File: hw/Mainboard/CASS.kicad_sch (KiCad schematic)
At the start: 22 parts, among them J27 CASS_A_HEADER, J28 CASS_B_HEADER, J5 CASS A, J6 CASS B, Q1 AO3401A, Q3 AO3401A

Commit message: hw: add more Mouse part numbers
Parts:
- J27, J28: MOUSER (none) -> 649-1012937893602BLF
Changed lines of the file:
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@@
+      (effects (font (size 1.27 1.27)) hide)
+    )
+    (property "MOUSER" "649-1012937893602BLF" (id 4) (at 195.58 44.45 0)
       (effects (font (size 1.27 1.27)) hide)
     )
@@
       (effects (font (size 1.27 1.27)) hide)
     )
+    (property "MOUSER" "649-1012937893602BLF" (id 4) (at 241.3 44.45 0)
+      (effects (font (size 1.27 1.27)) hide)
+    )

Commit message: hw: 9V DC plug on left edge, change default track size
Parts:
- renumbered D6 to D12, D7 to D13, J27 to J14, J28 to J15, J5 to J16, J6 to J17, JP5 to JP2, JP6 to JP3, JP3 to JP4, JP4 to JP5, JP1 to JP6, JP2 to JP7, PT21 to PT38, PT15 to PT39, PT16 to PT40, PT22 to PT41, Q3 to Q2, Q1 to Q3, R50 to R31, R56 to R32, R49 to R33, R44 to R34
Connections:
- net VCC1: now reaches PT39.2, R32.1
- net VCC2: now reaches PT40.2, R33.1
- net CASS_A_~{MOTOR}: now reaches D12.1 (K), JP2.2 (C)
- net CASS_B_~{MOTOR}: now reaches D13.1 (K), JP3.2 (C)

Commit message: hw: 25x2 header (wip)
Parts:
- renumbered J14 to J15, J15 to J16, J16 to J17, J17 to J18
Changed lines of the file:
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@@
   (symbol (lib_id "Retrocomputing:CBM_PET_CASS_Conn_01x06_Card_Edge") (at 242.57 142.24 0) (unit 1)
     (in_bom yes) (on_board yes)
-    (property "Reference" "J17" (id 0) (at 247.142 142.4432 0)
+    (property "Reference" "J18" (id 0) (at 247.142 142.4432 0)
       (effects (font (size 1.27 1.27)) (justify left))
     )
@@
   (symbol (lib_name "CBM_PET_CASS_Conn_01x06_Card_Edge_1") (lib_id "Retrocomputing:CBM_PET_CASS_Conn_01x06_Card_Edge") (at 242.57 100.33 0) (unit 1)
     (in_bom yes) (on_board yes)
-    (property "Reference" "J16" (id 0) (at 247.142 100.5332 0)
+    (property "Reference" "J17" (id 0) (at 247.142 100.5332 0)
       (effects (font (size 1.27 1.27)) (justify left))
     )
@@
   (symbol (lib_id "Connector:Conn_01x06_Male") (at 195.58 44.45 0) (mirror y) (unit 1)
     (in_bom yes) (on_board yes) (fields_autoplaced)
-    (property "Reference" "J14" (id 0) (at 196.85 44.4499 0)
+    (property "Reference" "J15" (id 0) (at 196.85 44.4499 0)
       (effects (font (size 1.27 1.27)) (justify right))
     )
@@
   (symbol (lib_id "PET:PD_GND") (at 250.19 34.29 0) (unit 1)
     (in_bom yes) (on_board yes) (fields_autoplaced)
-    (property "Reference" "#PWR0109" (id 0) (at 250.19 40.64 0)
+    (property "Reference" "#PWR0111" (id 0) (at 250.19 40.64 0)
       (effects (font (size 1.27 1.27)) hide)
     )
@@
   (symbol (lib_id "PET:PD_GND") (at 251.46 90.17 0) (unit 1)
     (in_bom yes) (on_board yes) (fields_autoplaced)
-    (property "Reference" "#PWR0111" (id 0) (at 251.46 96.52 0)
+    (property "Reference" "#PWR0113" (id 0) (at 251.46 96.52 0)
       (effects (font (size 1.27 1.27)) hide)
     )
@@
   (symbol (lib_id "power:+5V") (at 186.69 34.29 0) (unit 1)
     (in_bom yes) (on_board yes) (fields_autoplaced)
-    (property "Reference" "#PWR0106" (id 0) (at 186.69 38.1 0)
+    (property "Reference" "#PWR0108" (id 0) (at 186.69 38.1 0)
       (effects (font (size 1.27 1.27)) hide)
     )
@@
   (symbol (lib_id "PET:PD_GND") (at 251.46 132.08 0) (unit 1)
     (in_bom yes) (on_board yes) (fields_autoplaced)
-    (property "Reference" "#PWR0115" (id 0) (at 251.46 138.43 0)
+    (property "Reference" "#PWR0117" (id 0) (at 251.46 138.43 0)
       (effects (font (size 1.27 1.27)) hide)
     )
@@
   (symbol (lib_id "power:+5V") (at 233.68 132.08 0) (unit 1)
     (in_bom yes) (on_board yes) (fields_autoplaced)
-    (property "Reference" "#PWR0114" (id 0) (at 233.68 135.89 0)
+    (property "Reference" "#PWR0116" (id 0) (at 233.68 135.89 0)
       (effects (font (size 1.27 1.27)) hide)
     )
@@
   (symbol (lib_id "power:+5V") (at 232.41 34.29 0) (unit 1)
     (in_bom yes) (on_board yes) (fields_autoplaced)
-    (property "Reference" "#PWR0108" (id 0) (at 232.41 38.1 0)
+    (property "Reference" "#PWR0110" (id 0) (at 232.41 38.1 0)
       (effects (font (size 1.27 1.27)) hide)
     )
@@
   (symbol (lib_id "Connector:Conn_01x06_Male") (at 241.3 44.45 0) (mirror y) (unit 1)
     (in_bom yes) (on_board yes) (fields_autoplaced)
-    (property "Reference" "J15" (id 0) (at 242.57 44.4499 0)
+    (property "Reference" "J16" (id 0) (at 242.57 44.4499 0)
       (effects (font (size 1.27 1.27)) (justify right))
     )
@@
   (symbol (lib_id "power:+6V") (at 203.2 133.35 0) (unit 1)
     (in_bom yes) (on_board yes) (fields_autoplaced)
-    (property "Reference" "#PWR0116" (id 0) (at 203.2 137.16 0)
+    (property "Reference" "#PWR0118" (id 0) (at 203.2 137.16 0)
       (effects (font (size 1.27 1.27)) hide)
     )
@@
   (symbol (lib_id "PET:PD_GND") (at 204.47 34.29 0) (unit 1)
     (in_bom yes) (on_board yes) (fields_autoplaced)
-    (property "Reference" "#PWR0107" (id 0) (at 204.47 40.64 0)
+    (property "Reference" "#PWR0109" (id 0) (at 204.47 40.64 0)
       (effects (font (size 1.27 1.27)) hide)
     )
@@
   (symbol (lib_id "power:+6V") (at 203.2 91.44 0) (unit 1)
     (in_bom yes) (on_board yes) (fields_autoplaced)
-    (property "Reference" "#PWR0112" (id 0) (at 203.2 95.25 0)
+    (property "Reference" "#PWR0114" (id 0) (at 203.2 95.25 0)
       (effects (font (size 1.27 1.27)) hide)
     )
@@
   (symbol (lib_id "power:+5V") (at 233.68 90.17 0) (unit 1)
     (in_bom yes) (on_board yes) (fields_autoplaced)
-    (property "Reference" "#PWR0110" (id 0) (at 233.68 93.98 0)
+    (property "Reference" "#PWR0112" (id 0) (at 233.68 93.98 0)
       (effects (font (size 1.27 1.27)) hide)
     )
@@
   (symbol (lib_id "power:+5V") (at 35.56 106.68 0) (unit 1)
     (in_bom yes) (on_board yes) (fields_autoplaced)
-    (property "Reference" "#PWR0113" (id 0) (at 35.56 110.49 0)
-      (effects (font (size 1.27 1.27)) hide)
-    )
+    (property "Reference" "#PWR0115" (id 0) (at 35.56 110.49 0)
+      (effects (font (size 1.27 1.27)) hide)
+    )

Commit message: hw: 2x config switch (wip)
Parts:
- renumbered J15 to J14, J16 to J15, J17 to J16, J18 to J17
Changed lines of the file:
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@@
   (symbol (lib_id "Retrocomputing:CBM_PET_CASS_Conn_01x06_Card_Edge") (at 242.57 142.24 0) (unit 1)
     (in_bom yes) (on_board yes)
-    (property "Reference" "J18" (id 0) (at 247.142 142.4432 0)
+    (property "Reference" "J17" (id 0) (at 247.142 142.4432 0)
       (effects (font (size 1.27 1.27)) (justify left))
     )
@@
   (symbol (lib_name "CBM_PET_CASS_Conn_01x06_Card_Edge_1") (lib_id "Retrocomputing:CBM_PET_CASS_Conn_01x06_Card_Edge") (at 242.57 100.33 0) (unit 1)
     (in_bom yes) (on_board yes)
-    (property "Reference" "J17" (id 0) (at 247.142 100.5332 0)
+    (property "Reference" "J16" (id 0) (at 247.142 100.5332 0)
       (effects (font (size 1.27 1.27)) (justify left))
     )
@@
   (symbol (lib_id "Connector:Conn_01x06_Male") (at 195.58 44.45 0) (mirror y) (unit 1)
     (in_bom yes) (on_board yes) (fields_autoplaced)
-    (property "Reference" "J15" (id 0) (at 196.85 44.4499 0)
+    (property "Reference" "J14" (id 0) (at 196.85 44.4499 0)
       (effects (font (size 1.27 1.27)) (justify right))
     )
@@
   (symbol (lib_id "PET:PD_GND") (at 250.19 34.29 0) (unit 1)
     (in_bom yes) (on_board yes) (fields_autoplaced)
-    (property "Reference" "#PWR0111" (id 0) (at 250.19 40.64 0)
+    (property "Reference" "#PWR0117" (id 0) (at 250.19 40.64 0)
       (effects (font (size 1.27 1.27)) hide)
     )
@@
   (symbol (lib_id "PET:PD_GND") (at 251.46 90.17 0) (unit 1)
     (in_bom yes) (on_board yes) (fields_autoplaced)
-    (property "Reference" "#PWR0113" (id 0) (at 251.46 96.52 0)
+    (property "Reference" "#PWR0119" (id 0) (at 251.46 96.52 0)
       (effects (font (size 1.27 1.27)) hide)
     )
@@
   (symbol (lib_id "power:+5V") (at 186.69 34.29 0) (unit 1)
     (in_bom yes) (on_board yes) (fields_autoplaced)
-    (property "Reference" "#PWR0108" (id 0) (at 186.69 38.1 0)
+    (property "Reference" "#PWR0114" (id 0) (at 186.69 38.1 0)
       (effects (font (size 1.27 1.27)) hide)
     )
@@
   (symbol (lib_id "PET:PD_GND") (at 251.46 132.08 0) (unit 1)
     (in_bom yes) (on_board yes) (fields_autoplaced)
-    (property "Reference" "#PWR0117" (id 0) (at 251.46 138.43 0)
+    (property "Reference" "#PWR0123" (id 0) (at 251.46 138.43 0)
       (effects (font (size 1.27 1.27)) hide)
     )
@@
   (symbol (lib_id "power:+5V") (at 233.68 132.08 0) (unit 1)
     (in_bom yes) (on_board yes) (fields_autoplaced)
-    (property "Reference" "#PWR0116" (id 0) (at 233.68 135.89 0)
+    (property "Reference" "#PWR0122" (id 0) (at 233.68 135.89 0)
       (effects (font (size 1.27 1.27)) hide)
     )
@@
   (symbol (lib_id "power:+5V") (at 232.41 34.29 0) (unit 1)
     (in_bom yes) (on_board yes) (fields_autoplaced)
-    (property "Reference" "#PWR0110" (id 0) (at 232.41 38.1 0)
+    (property "Reference" "#PWR0116" (id 0) (at 232.41 38.1 0)
       (effects (font (size 1.27 1.27)) hide)
     )
@@
   (symbol (lib_id "Connector:Conn_01x06_Male") (at 241.3 44.45 0) (mirror y) (unit 1)
     (in_bom yes) (on_board yes) (fields_autoplaced)
-    (property "Reference" "J16" (id 0) (at 242.57 44.4499 0)
+    (property "Reference" "J15" (id 0) (at 242.57 44.4499 0)
       (effects (font (size 1.27 1.27)) (justify right))
     )
@@
   (symbol (lib_id "power:+6V") (at 203.2 133.35 0) (unit 1)
     (in_bom yes) (on_board yes) (fields_autoplaced)
-    (property "Reference" "#PWR0118" (id 0) (at 203.2 137.16 0)
+    (property "Reference" "#PWR0124" (id 0) (at 203.2 137.16 0)
       (effects (font (size 1.27 1.27)) hide)
     )
@@
   (symbol (lib_id "PET:PD_GND") (at 204.47 34.29 0) (unit 1)
     (in_bom yes) (on_board yes) (fields_autoplaced)
-    (property "Reference" "#PWR0109" (id 0) (at 204.47 40.64 0)
+    (property "Reference" "#PWR0115" (id 0) (at 204.47 40.64 0)
       (effects (font (size 1.27 1.27)) hide)
     )
@@
   (symbol (lib_id "power:+6V") (at 203.2 91.44 0) (unit 1)
     (in_bom yes) (on_board yes) (fields_autoplaced)
-    (property "Reference" "#PWR0114" (id 0) (at 203.2 95.25 0)
+    (property "Reference" "#PWR0120" (id 0) (at 203.2 95.25 0)
       (effects (font (size 1.27 1.27)) hide)
     )
@@
   (symbol (lib_id "power:+5V") (at 233.68 90.17 0) (unit 1)
     (in_bom yes) (on_board yes) (fields_autoplaced)
-    (property "Reference" "#PWR0112" (id 0) (at 233.68 93.98 0)
+    (property "Reference" "#PWR0118" (id 0) (at 233.68 93.98 0)
       (effects (font (size 1.27 1.27)) hide)
     )
@@
   (symbol (lib_id "power:+5V") (at 35.56 106.68 0) (unit 1)
     (in_bom yes) (on_board yes) (fields_autoplaced)
-    (property "Reference" "#PWR0115" (id 0) (at 35.56 110.49 0)
-      (effects (font (size 1.27 1.27)) hide)
-    )
+    (property "Reference" "#PWR0121" (id 0) (at 35.56 110.49 0)
+      (effects (font (size 1.27 1.27)) hide)
+    )

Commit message: hw: touch ups (wip)
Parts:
- added C99: 10u, Capacitor_SMD:C_0603_1608Metric, symbol Device:C_Small
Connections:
- net +5V: now also C99.2
- net PD_GND: now also C99.1
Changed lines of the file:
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@@
+    (pin "1")
+  )
+  (symbol (lib_id "PET:PD_GND") (at 41.91 180.34 0) (unit 1)
+    (in_bom yes) (on_board yes) (fields_autoplaced)
+    (property "Reference" "#PWR0177" (id 0) (at 41.91 186.69 0)
+      (effects (font (size 1.27 1.27)) hide)
+    )
+    (property "Value" "PD_GND" (id 1) (at 41.91 185.42 0))
+    (property "Footprint" "" (id 2) (at 41.91 180.34 0)
+      (effects (font (size 1.27 1.27)) hide)
+    )
+    (property "Datasheet" "" (id 3) (at 41.91 180.34 0)
+      (effects (font (size 1.27 1.27)) hide)
+    )
     (pin "1")
   )
@@
     (pin "5")
     (pin "6")
+  )
+  (symbol (lib_id "power:+5V") (at 41.91 175.26 0) (unit 1)
+    (in_bom yes) (on_board yes) (fields_autoplaced)
+    (property "Reference" "#PWR0176" (id 0) (at 41.91 179.07 0)
+      (effects (font (size 1.27 1.27)) hide)
+    )
+    (property "Value" "+5V" (id 1) (at 41.91 170.18 0))
+    (property "Footprint" "" (id 2) (at 41.91 175.26 0)
+      (effects (font (size 1.27 1.27)) hide)
+    )
+    (property "Datasheet" "" (id 3) (at 41.91 175.26 0)
+      (effects (font (size 1.27 1.27)) hide)
+    )
+    (pin "1")
   )
   (symbol (lib_id "Device:R_Small") (at 195.58 138.43 0) (unit 1)
@@
     (pin "1")
   )
+  (symbol (lib_id "Device:C_Small") (at 41.91 177.8 0) (mirror x) (unit 1)
+    (in_bom yes) (on_board yes)
+    (property "Reference" "C99" (id 0) (at 44.2468 178.9684 0)
+      (effects (font (size 1.27 1.27)) (justify left))
+    )
+    (property "Value" "10u" (id 1) (at 44.2468 176.657 0)
+      (effects (font (size 1.27 1.27)) (justify left))
+    )
+    (property "Footprint" "Capacitor_SMD:C_0603_1608Metric" (id 2) (at 41.91 177.8 0)
+      (effects (font (size 1.27 1.27)) hide)
+    )
+    (property "Datasheet" "https://datasheet.lcsc.com/lcsc/2304140030_Samsung-Electro-Mechanics-CL10A106MA8NRNC_C96446.pdf" (id 3) (at 41.91 177.8 0)
+      (effects (font (size 1.27 1.27)) hide)
+    )
+    (property "LCSC" "C96446" (id 4) (at 41.91 177.8 0)
+      (effects (font (size 1.27 1.27)) hide)
+    )
+    (pin "1")
+    (pin "2")
+  )
   (symbol (lib_name "SolderJumper_3_Open_3") (lib_id "Jumper:SolderJumper_3_Open") (at 151.13 54.61 0) (unit 1)

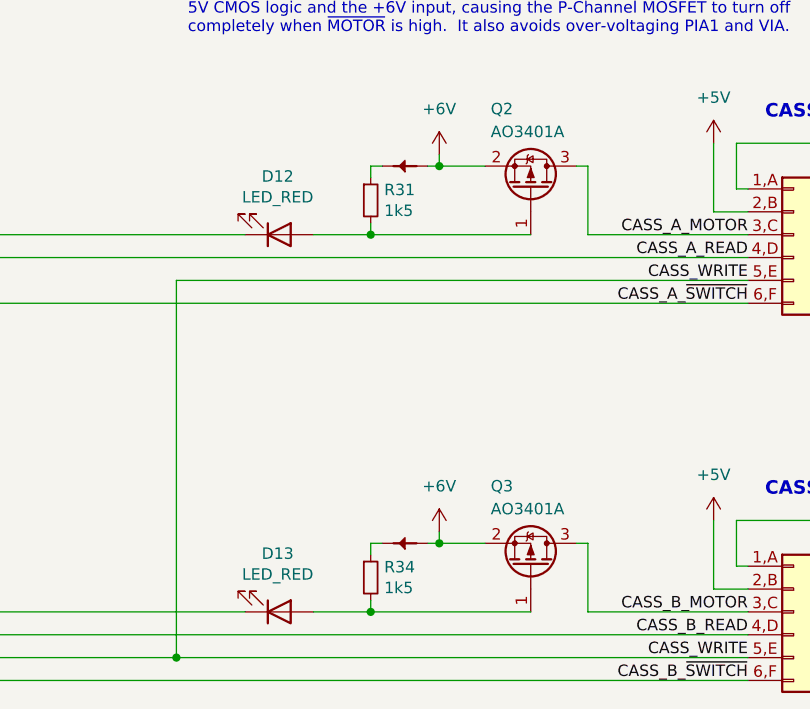
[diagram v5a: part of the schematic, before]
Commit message: hw: routing touchups (wip)
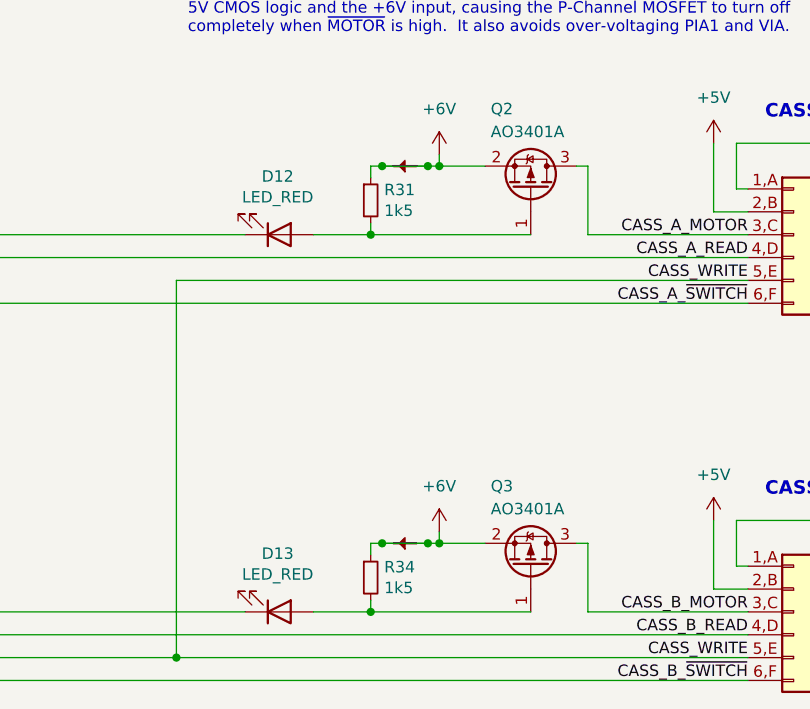
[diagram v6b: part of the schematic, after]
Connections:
- net +6V: now also PT38.2, PT41.2, R31.1, R34.1
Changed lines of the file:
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@@
   (junction (at 45.72 93.98) (diameter 0) (color 0 0 0 0)
   )
+  (junction (at 196.85 134.62) (diameter 0) (color 0 0 0 0)
+  )
   (junction (at 102.87 74.93) (diameter 0) (color 0 0 0 0)
   )
@@
   (junction (at 195.58 100.33) (diameter 0) (color 0 0 0 0)
   )
+  (junction (at 196.85 92.71) (diameter 0) (color 0 0 0 0)
+  )
   (junction (at 64.77 93.98) (diameter 0) (color 0 0 0 0)
   )
   (junction (at 195.58 142.24) (diameter 0) (color 0 0 0 0)
   )
+  (junction (at 201.93 134.62) (diameter 0) (color 0 0 0 0)
+  )
   (junction (at 121.92 54.61) (diameter 0) (color 0 0 0 0)
   )
+  (junction (at 201.93 92.71) (diameter 0) (color 0 0 0 0)
+  )
   (junction (at 83.82 74.93) (diameter 0) (color 0 0 0 0)
   )
@@
     (stroke (width 0) (type default) (color 0 0 0 0))
   )
+  (wire (pts (xy 196.85 134.62) (xy 201.93 134.62))
+    (stroke (width 0) (type default) (color 0 0 0 0))
+  )
   (wire (pts (xy 195.58 134.62) (xy 196.85 134.62))
     (stroke (width 0) (type default) (color 0 0 0 0))
@@
     (stroke (width 0) (type default) (color 0 0 0 0))
   )
+  (wire (pts (xy 196.85 92.71) (xy 201.93 92.71))
+    (stroke (width 0) (type default) (color 0 0 0 0))
+  )

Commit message: hw: touchups (wip)
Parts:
- JP2, JP3, JP4, JP5, JP6, JP7: footprint Jumper:SolderJumper-3_P1.3mm_Open_RoundedPad1.0x1.5mm -> Jumper:SolderJumper-3_P1.3mm_Bridged12_RoundedPad1.0x1.5mm
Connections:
- net VCC1 is gone; now on net +5V: PT39.2, R32.1
- net VCC2 is gone; now on net +5V: PT40.2, R33.1
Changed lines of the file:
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@@
   (junction (at 203.2 92.71) (diameter 0) (color 0 0 0 0)
   )
+  (junction (at 41.91 113.03) (diameter 0) (color 0 0 0 0)
+  )
   (junction (at 35.56 107.95) (diameter 0) (color 0 0 0 0)
   )
@@
   (junction (at 195.58 142.24) (diameter 0) (color 0 0 0 0)
   )
+  (junction (at 41.91 107.95) (diameter 0) (color 0 0 0 0)
+  )
   (junction (at 201.93 134.62) (diameter 0) (color 0 0 0 0)
   )
+  (junction (at 36.83 113.03) (diameter 0) (color 0 0 0 0)
+  )
   (junction (at 121.92 54.61) (diameter 0) (color 0 0 0 0)
   )
@@
   (junction (at 54.61 107.95) (diameter 0) (color 0 0 0 0)
   )
+  (junction (at 36.83 107.95) (diameter 0) (color 0 0 0 0)
+  )
   (junction (at 140.97 54.61) (diameter 0) (color 0 0 0 0)
   )
@@
     (stroke (width 0) (type default) (color 0 0 0 0))
   )
+  (wire (pts (xy 36.83 113.03) (xy 41.91 113.03))
+    (stroke (width 0) (type default) (color 0 0 0 0))
+  )
   (wire (pts (xy 189.23 39.37) (xy 189.23 34.29))
     (stroke (width 0) (type default) (color 0 0 0 0))
@@
   )
   (wire (pts (xy 189.23 34.29) (xy 204.47 34.29))
+    (stroke (width 0) (type default) (color 0 0 0 0))
+  )
+  (wire (pts (xy 36.83 107.95) (xy 41.91 107.95))
     (stroke (width 0) (type default) (color 0 0 0 0))
   )
@@
     (property "Reference" "JP2" (id 0) (at 130.81 49.53 0))
     (property "Value" "CASS A ~{MOTOR}" (id 1) (at 130.81 52.07 0))
-    (property "Footprint" "Jumper:SolderJumper-3_P1.3mm_Open_RoundedPad1.0x1.5mm" (id 2) (at 130.81 54.61 0)
+    (property "Footprint" "Jumper:SolderJumper-3_P1.3mm_Bridged12_RoundedPad1.0x1.5mm" (id 2) (at 130.81 54.61 0)
       (effects (font (size 1.27 1.27)) hide)
     )
@@
     (property "Reference" "JP6" (id 0) (at 54.61 88.9 0))
     (property "Value" "CASS A ~{SWITCH}" (id 1) (at 54.61 91.44 0))
-    (property "Footprint" "Jumper:SolderJumper-3_P1.3mm_Open_RoundedPad1.0x1.5mm" (id 2) (at 54.61 93.98 0)
+    (property "Footprint" "Jumper:SolderJumper-3_P1.3mm_Bridged12_RoundedPad1.0x1.5mm" (id 2) (at 54.61 93.98 0)
       (effects (font (size 1.27 1.27)) hide)
     )
@@
     (property "Reference" "JP4" (id 0) (at 92.71 69.85 0))
     (property "Value" "CASS A READ" (id 1) (at 92.71 72.39 0))
-    (property "Footprint" "Jumper:SolderJumper-3_P1.3mm_Open_RoundedPad1.0x1.5mm" (id 2) (at 92.71 74.93 0)
+    (property "Footprint" "Jumper:SolderJumper-3_P1.3mm_Bridged12_RoundedPad1.0x1.5mm" (id 2) (at 92.71 74.93 0)
       (effects (font (size 1.27 1.27)) hide)
     )
@@
     (property "Reference" "JP7" (id 0) (at 74.93 88.9 0))
     (property "Value" "CASS B ~{SWITCH}" (id 1) (at 74.93 91.44 0))
-    (property "Footprint" "Jumper:SolderJumper-3_P1.3mm_Open_RoundedPad1.0x1.5mm" (id 2) (at 74.93 93.98 0)
+    (property "Footprint" "Jumper:SolderJumper-3_P1.3mm_Bridged12_RoundedPad1.0x1.5mm" (id 2) (at 74.93 93.98 0)
       (effects (font (size 1.27 1.27)) hide)
     )
@@
     (property "Reference" "JP3" (id 0) (at 151.13 49.53 0))
     (property "Value" "CASS B ~{MOTOR}" (id 1) (at 151.13 52.07 0))
-    (property "Footprint" "Jumper:SolderJumper-3_P1.3mm_Open_RoundedPad1.0x1.5mm" (id 2) (at 151.13 54.61 0)
+    (property "Footprint" "Jumper:SolderJumper-3_P1.3mm_Bridged12_RoundedPad1.0x1.5mm" (id 2) (at 151.13 54.61 0)
       (effects (font (size 1.27 1.27)) hide)
     )
@@
     (property "Reference" "JP5" (id 0) (at 113.03 69.85 0))
     (property "Value" "CASS B READ" (id 1) (at 113.03 72.39 0))
-    (property "Footprint" "Jumper:SolderJumper-3_P1.3mm_Open_RoundedPad1.0x1.5mm" (id 2) (at 113.03 74.93 0)
-      (effects (font (size 1.27 1.27)) hide)
-    )
+    (property "Footprint" "Jumper:SolderJumper-3_P1.3mm_Bridged12_RoundedPad1.0x1.5mm" (id 2) (at 113.03 74.93 0)
+      (effects (font (size 1.27 1.27)) hide)
+    )
